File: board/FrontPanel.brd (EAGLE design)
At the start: 76.2 x 44.5 mm, 10 parts, among them J1 PINHD-1X2BIG

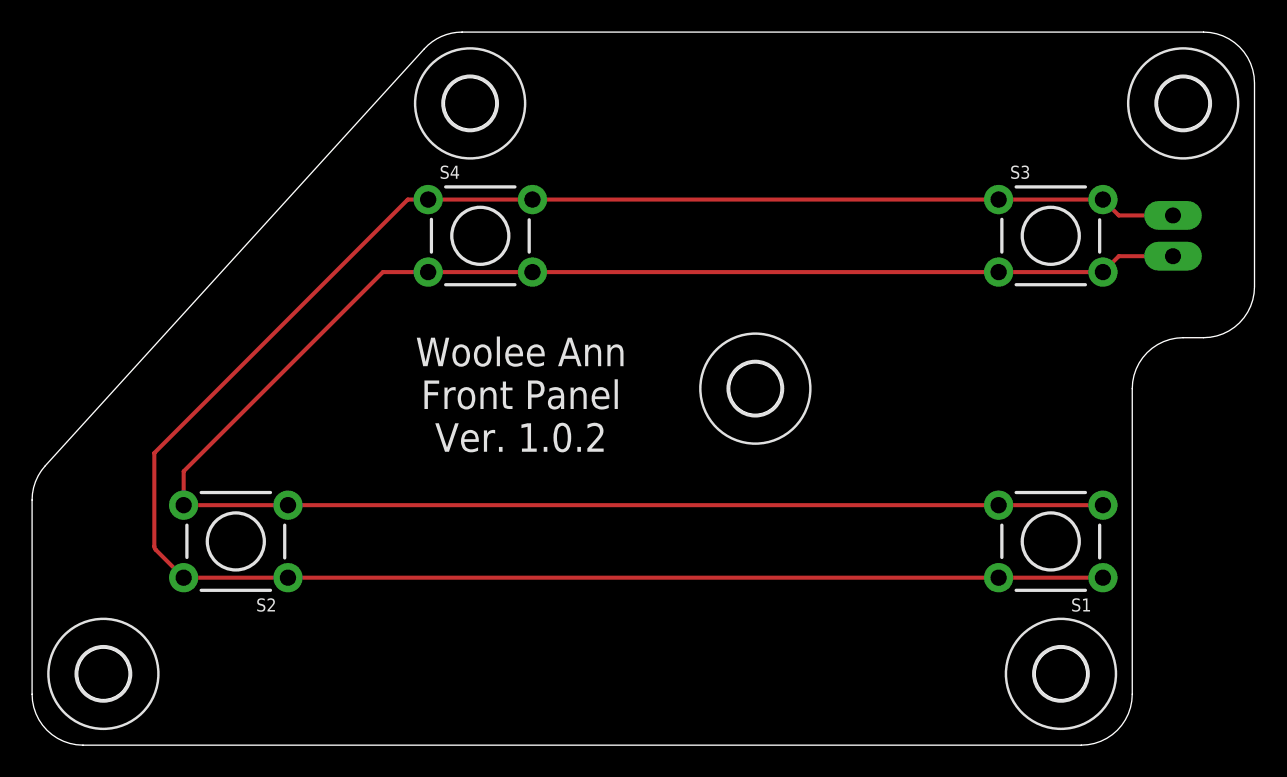
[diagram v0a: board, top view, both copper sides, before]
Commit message: Add hole to front panel
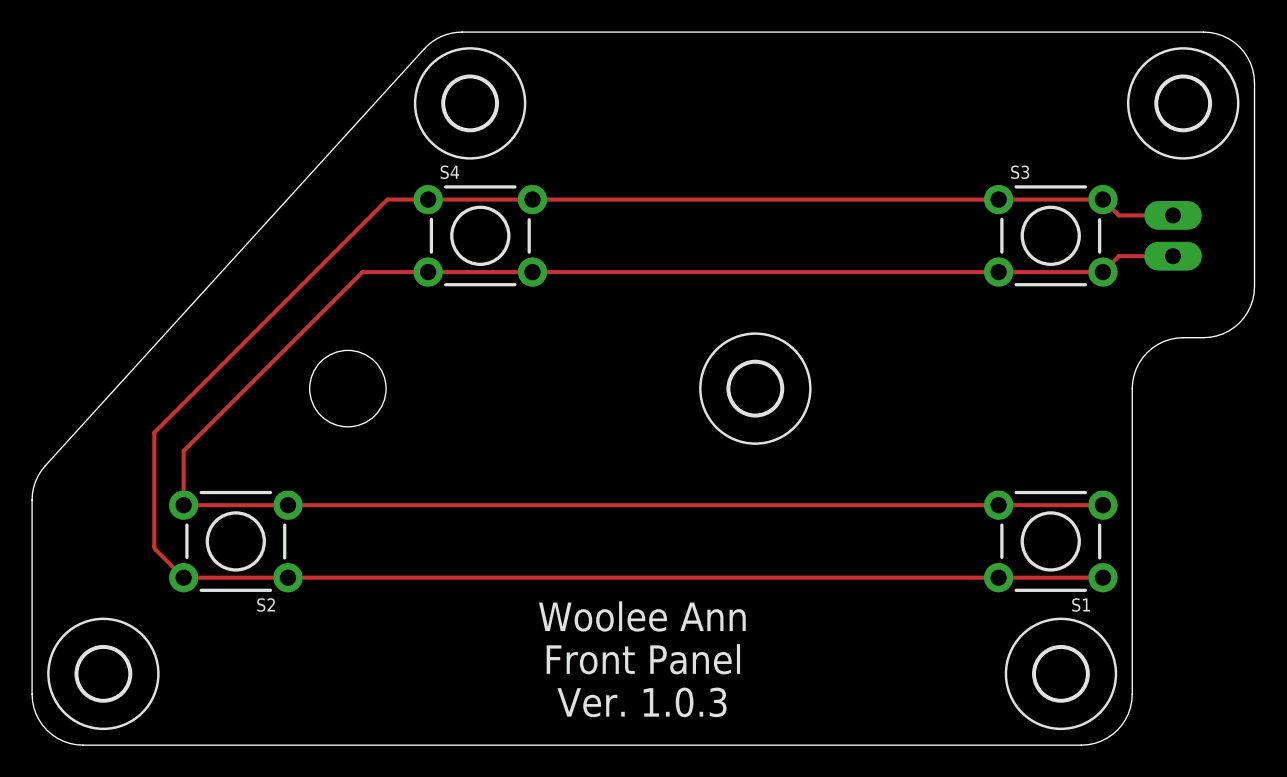
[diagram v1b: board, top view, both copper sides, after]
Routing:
- net N$2: track 126.7 -> 127.5 mm
- net N$1: track 136.3 -> 137.0 mm
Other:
- board text added: "Woolee Ann Front Panel Ver. 1.0.3"
- board text removed: "Woolee Ann Front Panel Ver. 1.0.2"
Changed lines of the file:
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@@
 <?xml version="1.0" encoding="utf-8"?>
 <!DOCTYPE eagle SYSTEM "eagle.dtd">
-<eagle version="7.4.0">
+<eagle version="7.5.0">
 <drawing>
 <settings>
@@
 <setting verticaltext="up"/>
 </settings>
-<grid distance="0.05" unitdist="inch" unit="inch" style="lines" multiple="2" display="yes" altdistance="0.025" altunitdist="inch" altunit="inch"/>
+<grid distance="0.1" unitdist="inch" unit="inch" style="lines" multiple="1" display="yes" altdistance="0.025" altunitdist="inch" altunit="inch"/>
 <layers>
 <layer number="1" name="Top" color="4" fill="1" visible="yes" active="yes"/>
@@
 <text x="71.12" y="34.29" size="1.016" layer="122" rot="MR0" align="bottom-center">RUN/STOP</text>
 <text x="71.12" y="27.94" size="1.016" layer="122" rot="MR0" align="bottom-center">GND</text>
-<text x="30.48" y="25.4" size="1.778" layer="121" align="top-center">Woolee Ann
+<text x="38.1" y="8.89" size="1.778" layer="121" align="top-center">Woolee Ann
 Front Panel
-Ver. 1.0.2</text>
+Ver. 1.0.3</text>
+<hole x="19.685" y="22.225" drill="4.7625"/>
 </plain>
 <attributes>
@@
 <wire x1="60.2488" y1="34.0106" x2="31.1912" y2="34.0106" width="0.254" layer="1"/>
 <wire x1="31.1912" y1="34.0106" x2="24.6888" y2="34.0106" width="0.254" layer="1"/>
-<wire x1="7.62" y1="18.2118" x2="7.62" y2="12.3997125" width="0.254" layer="1"/>
+<wire x1="7.62" y1="19.4818" x2="7.62" y2="12.3997125" width="0.254" layer="1"/>
 <wire x1="7.62" y1="12.3997125" x2="7.71299375" y2="12.17520625" width="0.254" layer="1" curve="45"/>
 <wire x1="7.71299375" y1="12.17520625" x2="9.4488" y2="10.4394" width="0.254" layer="1"/>
@@
 <wire x1="71.12" y1="33.02" x2="67.7418" y2="33.02" width="0.254" layer="1"/>
 <wire x1="67.7418" y1="33.02" x2="66.7512" y2="34.0106" width="0.254" layer="1"/>
-<wire x1="24.6888" y1="34.0106" x2="23.4188" y2="34.0106" width="0.254" layer="1"/>
-<wire x1="23.4188" y1="34.0106" x2="7.62" y2="18.2118" width="0.254" layer="1"/>
+<wire x1="24.6888" y1="34.0106" x2="22.1488" y2="34.0106" width="0.254" layer="1"/>
+<wire x1="22.1488" y1="34.0106" x2="7.62" y2="19.4818" width="0.254" layer="1"/>
 </signal>
 <signal name="N$2">
@@
 <wire x1="71.12" y1="30.48" x2="67.7418" y2="30.48" width="0.254" layer="1"/>
 <wire x1="67.7418" y1="30.48" x2="66.7512" y2="29.4894" width="0.254" layer="1"/>
-<wire x1="24.6888" y1="29.4894" x2="21.8694" y2="29.4894" width="0.254" layer="1"/>
-<wire x1="9.4488" y1="17.0688" x2="9.4488" y2="14.9606" width="0.254" layer="1"/>
-<wire x1="21.8694" y1="29.4894" x2="9.4488" y2="17.0688" width="0.254" layer="1"/>
+<wire x1="24.6888" y1="29.4894" x2="20.5994" y2="29.4894" width="0.254" layer="1"/>
+<wire x1="9.4488" y1="18.3388" x2="9.4488" y2="14.9606" width="0.254" layer="1"/>
+<wire x1="20.5994" y1="29.4894" x2="9.4488" y2="18.3388" width="0.254" layer="1"/>
 </signal>
 </signals>
